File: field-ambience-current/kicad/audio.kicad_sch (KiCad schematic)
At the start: 20 parts, among them J6 Speaker L (PUI AS04008PS, 4R 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, J7 Speaker R (PUI AS04008PS, 4R 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, U3 PCM5102A I²S DAC (TSSOP-20), U4 PAM8403 Class-D Stereo Amp (S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

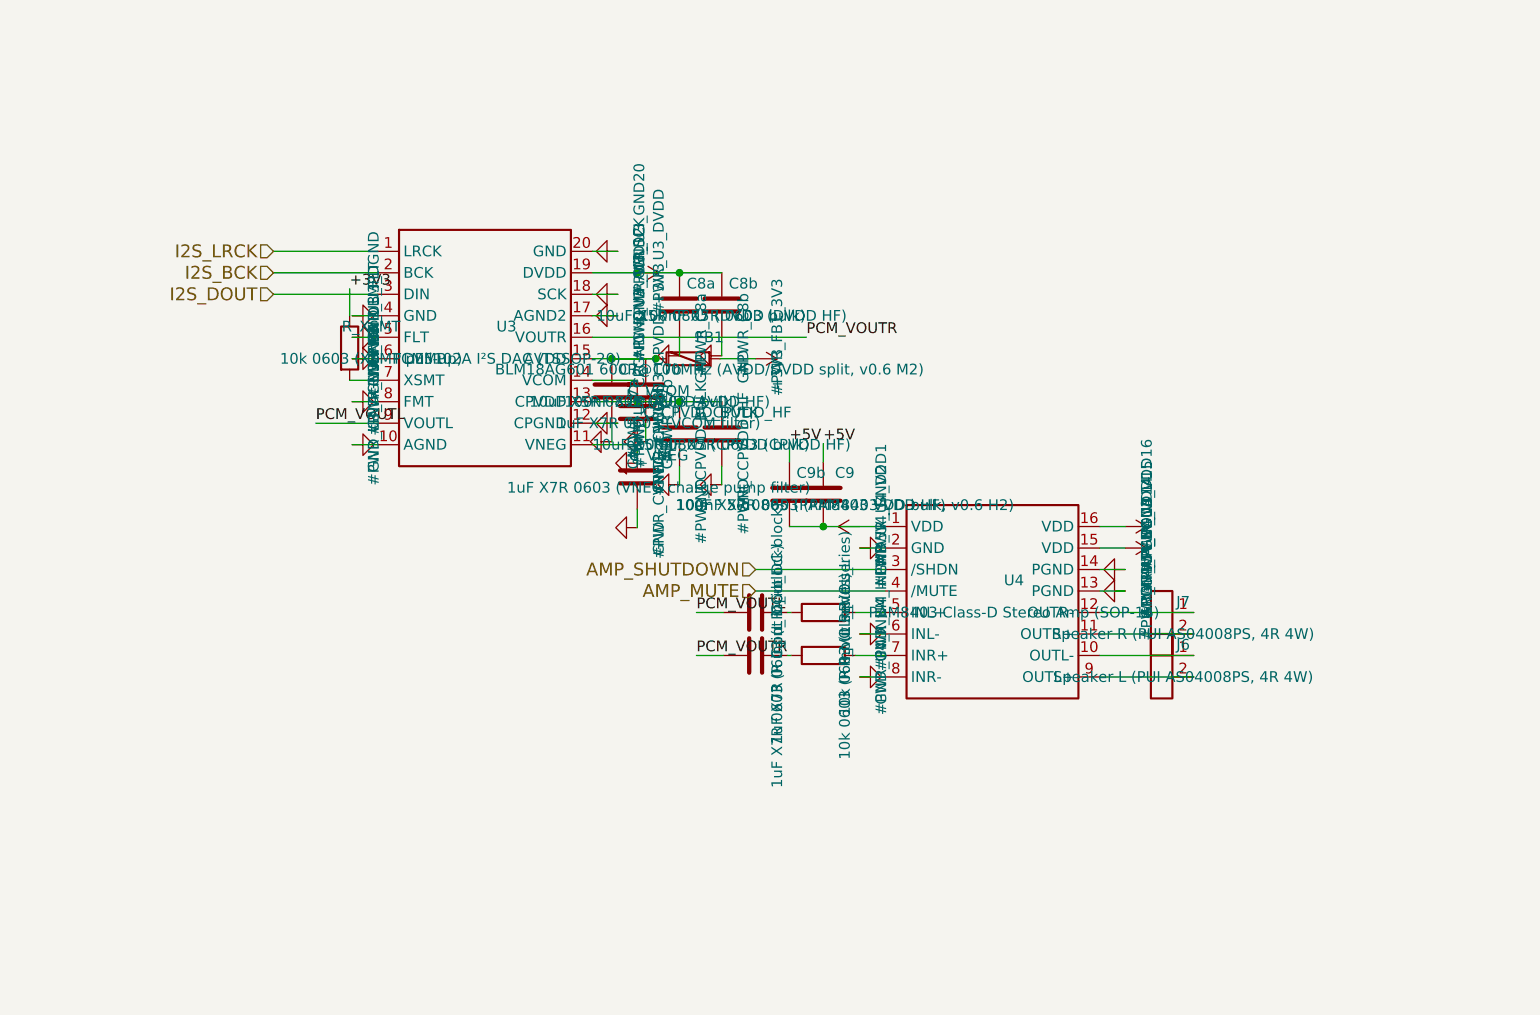
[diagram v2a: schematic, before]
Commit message: Fix PCM5102A and PAM8403 pinouts per official datasheets (Review Fix)
CRITICAL FIX from PR #1 review: Audio-IC symbols had invented pinouts
instead of official datasheet-correct mappings. Any PCB layout from
the previous version would have routed I²S, power and audio-out to
the wrong physical pads.

PCM5102A (TI SLAS859C, TSSOP-20) — corrected pinout:
  Old (wrong)              → New (per TI datasheet)
  Pin 1  = LRCK            → CPVDD
  Pin 2  = BCK             → CAPP (charge pump fly cap +)
  Pin 3  = DIN             → CPGND
  Pin 4  = GND             → CAPM (charge pump fly cap -)
  Pin 5  = FLT             → VNEG (1µF to GND)
  Pin 6  = DEMP            → OUTL (audio out left)
  Pin 7  = XSMT            → OUTR (audio out right)
  Pin 8  = FMT             → AVDD
  Pin 9  = VOUTL           → AGND
  Pin 10 = AGND            → DEMP
  Pin 11 = VNEG            → FLT
  Pin 12 = CPGND           → SCK (3-wire mode = GND)
  Pin 13 = CPVDD           → BCK (bit clock)
  Pin 14 = VCOM            → DIN (data in)
  Pin 15 = AVDD            → LRCK (left/right clock)
  Pin 16 = VOUTR           → FMT (I²S mode = GND)
  Pin 17 = AGND2           → XSMT (pull-up to DVDD)
  Pin 18 = SCK             → LDOO (LDO output, 100nF to GND)
  Pin 19 = DVDD            → DGND
  Pin 20 = GND             → DVDD

Audio Sheet rewritten with full TI reference design:
- CPVDD bulk+HF decoupling (10µF+100nF)
- CAPP-CAPM 1µF fly cap (charge pump)
- VNEG 1µF reservoir to GND
- AVDD via FB1 BLM18AG601 (v0.6 M2 split) + 10µF+100nF
- DVDD 10µF+100nF decoupling
- LDOO 100nF stability cap
- XSMT 10k pull-up to +3V3
- FLT, DEMP, SCK, FMT all tied to GND

PAM8403DR-H (Diodes Inc DS31295, SOIC-16, LCSC C17337) — corrected:
  Pin 1  = OUTL+        (BTL left output, positive)
  Pin 2  = PGND         (Power ground, left)
  Pin 3  = OUTL-        (BTL left output, negative)
  Pin 4  = PVDD         (Power supply, left)
  Pin 5  = /MUTE        (Active LOW mute)
  Pin 6  = VDD          (Internal supply)
  Pin 7  = INL 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
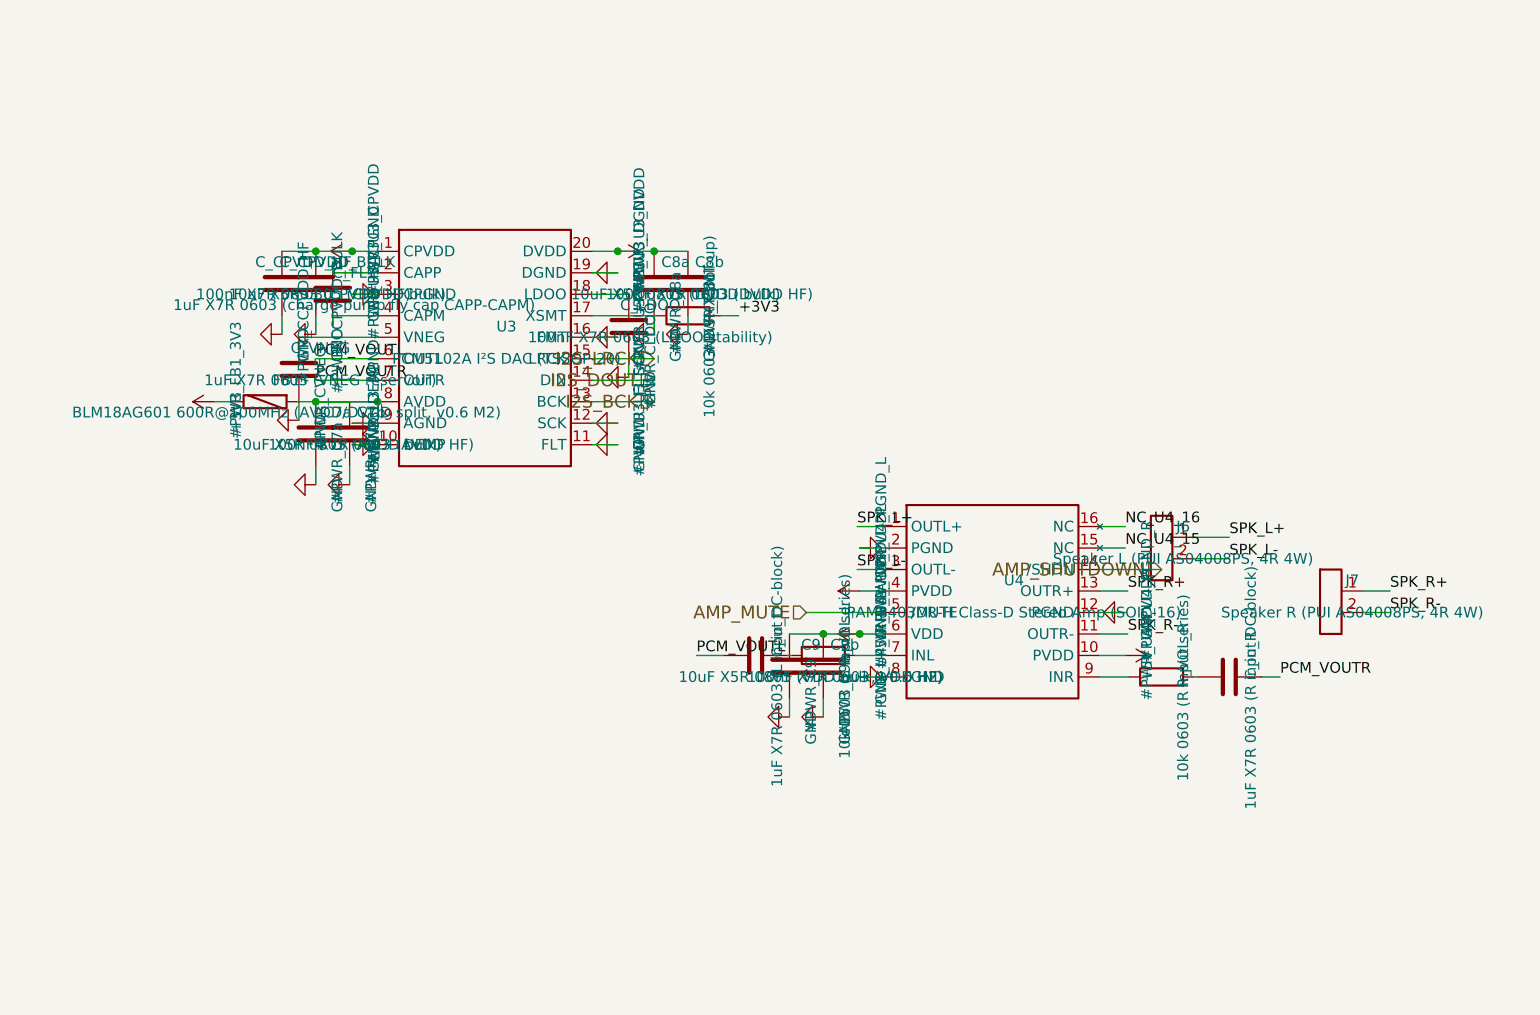
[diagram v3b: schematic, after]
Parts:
- removed C_VCOM: 1uF X7R 0603 (VCOM filter), Capacitor_SMD:C_0603_1608Metric, symbol Device:C
- added C_FLY: 1uF X7R 0603 (charge pump fly cap CAPP-CAPM), Capacitor_SMD:C_0603_1608Metric, symbol Device:C
- added C_LDOO: 100nF X7R 0603 (LDOO stability), Capacitor_SMD:C_0603_1608Metric, symbol Device:C
- C9: value 10uF X5R 0805 (PAM8403 VDD bulk, v0.6 H2) -> 10uF X5R 0805 (VDD bulk, v0.6 H2)
- C9b: value 100nF X7R 0603 (PAM8403 VDD HF) -> 100nF X7R 0603 (VDD HF)
- C_VNEG: value 1uF X7R 0603 (VNEG charge pump filter) -> 1uF X7R 0603 (VNEG reservoir)
- U3: MPN PCM5102A -> PCM5102APWR
- U4: value PAM8403 Class-D Stereo Amp (SOP-16) -> PAM8403DR-H Class-D Stereo Amp (SOIC-16); MPN PAM8403 -> PAM8403DR-H
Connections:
- net +3V3: now also FB1.2, R_XSMT.2, U3.1 (CPVDD), U3.20 (DVDD); no longer FB1.1, R_XSMT.1, U3.13 (CPVDD), U3.19 (DVDD)
- net +5V: now also U4.10 (PVDD), U4.4 (PVDD), U4.6 (VDD); no longer C9.2, C9b.2, U4.1 (VDD), U4.15 (VDD), U4.16 (VDD)
- net AMP_MUTE: now also U4.5 (/MUTE); no longer U4.4 (/MUTE)
- net AMP_SHUTDOWN: now also U4.14 (/SHDN); no longer U4.3 (/SHDN)
- net GND: now also C9.2, C9b.2, U3.16 (FMT), U3.19 (DGND), U3.3 (CPGND), U3.9 (AGND), U4.12 (PGND), C_LDOO.2; no longer C_VNEG.1, U3.17 (AGND2), U3.18 (SCK), U3.20 (GND), U3.4 (GND), U3.5 (FLT), U3.6 (DEMP), U3.8 (FMT), U4.13 (PGND), U4.14 (PGND), U4.6 (INL-)
- net I2S_BCK: now also U3.13 (BCK); no longer U3.2 (BCK)
- net I2S_DOUT: now also U3.14 (DIN); no longer U3.3 (DIN)
- net I2S_LRCK: now also U3.15 (LRCK); no longer U3.1 (LRCK)
- net PCM_VOUTL: now also U3.6 (OUTL); no longer U3.9 (VOUTL)
- net PCM_VOUTR: now also C_in_R.2, U3.7 (OUTR); no longer C_in_R.1, U3.16 (VOUTR)
- net SPK_L+: now reaches J6.1 (Pin_1)
- net SPK_L+: now also U4.1 (OUTL+); no longer U4.10 (OUTL-)
- net SPK_R-: now reaches J7.2 (Pin_2), U4.11 (OUTR-)
- net SPK_R+: now reaches J7.1 (Pin_1)
- net SPK_R+: now also U4.13 (OUTR+); no longer U4.12 (OUTR-)
- net at R_VOL_L.2: now also U4.7 (INL); no longer U4.5 (INL+)
- net at R_VOL_R.2: now also C_in_R.1; no longer U4.7 (INR+)
- net at U4.9 (INR): now also R_VOL_R.1; no longer J6.2 (Pin_2)
- net at C7a.1, C7b.1: now also FB1.1, U3.8 (AVDD); no longer FB1.2, U3.15 (AVDD)
- new net: C_FLY.1, U3.2 (CAPP)
- new net: C_FLY.2, U3.4 (CAPM)
- new net: C_VNEG.1, U3.5 (VNEG)
- new net: C_LDOO.1, U3.18 (LDOO)
- new net: R_XSMT.1, U3.17 (XSMT)
- new net NC_U4_15: U4.15 (NC)
- new net NC_U4_16: U4.16 (NC)
- new net SPK_L-: J6.2 (Pin_2), U4.3 (OUTL-)
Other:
- moved on the sheet: C7a, C7b, C8a, C8b, C9, C9b, C_CPVDD_BULK, C_CPVDD_HF, C_VNEG, C_in_L, C_in_R, FB1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

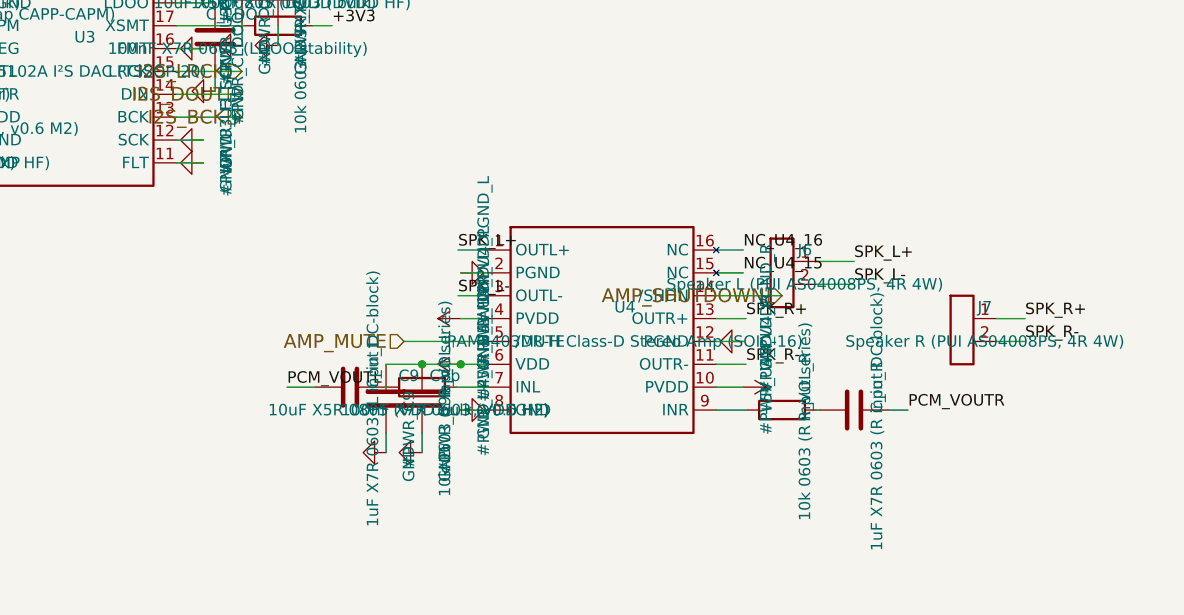
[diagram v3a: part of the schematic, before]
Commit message: Fix PAM8403H pinout using official datasheet PDF (PAM8403H.PDF)
The previous v0.6.1 fix for PAM8403 was based on a wrong DS31295
guess. With the actual Diodes Inc PAM8403H datasheet PDF now in the
repo (PAM8403H.PDF Rev 1-0 Nov 2012), the symbol can be verified
pin-by-pin against the JLCPCB C17337 part.

PAM8403H verified pinout (LCSC C17337):
  Pin 1:  -OUT_L (Left negative output, BTL)
  Pin 2:  PGND
  Pin 3:  +OUT_L (Left positive output, BTL)
  Pin 4:  PVDD
  Pin 5:  MUTE (active LOW)
  Pin 6:  VDD
  Pin 7:  INL
  Pin 8:  VREF  ← bypass cap to GND REQUIRED per datasheet
  Pin 9:  NC
  Pin 10: INR
  Pin 11: GND (analog)
  Pin 12: SHDN (active LOW)
  Pin 13: PVDD
  Pin 14: +OUT_R (Right positive output)
  Pin 15: PGND
  Pin 16: -OUT_R (Right negative output)

Critical errors fixed from v0.6.1:
- OUTL+ / OUTL- polarity was swapped (was on pins 1/3, must be 3/1)
- Pin 8 was wrongly GND, must be VREF (analog reference)
- Pin 9 was wrongly INR, must be NC
- Pin 10 was wrongly PVDD, must be INR
- Pin 11 was wrongly OUTR-, must be GND
- Pin 12 was wrongly PGND, must be SHDN
- Pin 13 was wrongly OUTR+, must be PVDD
- Pin 14 was wrongly /SHDN, must be +OUT_R
- Pin 15 was wrongly NC, must be PGND
- Pin 16 was wrongly NC, must be -OUT_R
- VREF bypass cap was missing — added C_VREF 1µF X7R

audio.kicad_sch U4 wiring completely rewritten to match correct pins.
Component count grew from 84 → 85 (added C_VREF).

SPEC v0.6.2 errata section updated with full PAM8403H pin table.

Verified via analyzer pin_nets dump for U4:
  Pin 1=SPK_L-, Pin 3=SPK_L+, Pin 14=SPK_R+, Pin 16=SPK_R-,
  Pin 4/6/13=+5V, Pin 2/11/15=GND, Pin 5=AMP_MUTE, Pin 12=AMP_SHUTDOWN,
  Pin 7/10=INL/INR, Pin 8=VREF (with C_VREF), Pin 9=NC.

Status: 0 functional errors, 19 warnings, 3 VM-001 false positives.
85 components, 117 nets. Audio path now safe for PCB layout once
mechanical footprint of SOP-16/SOIC-16 is also verified against the
exact JLC-shipped PAM8403H.
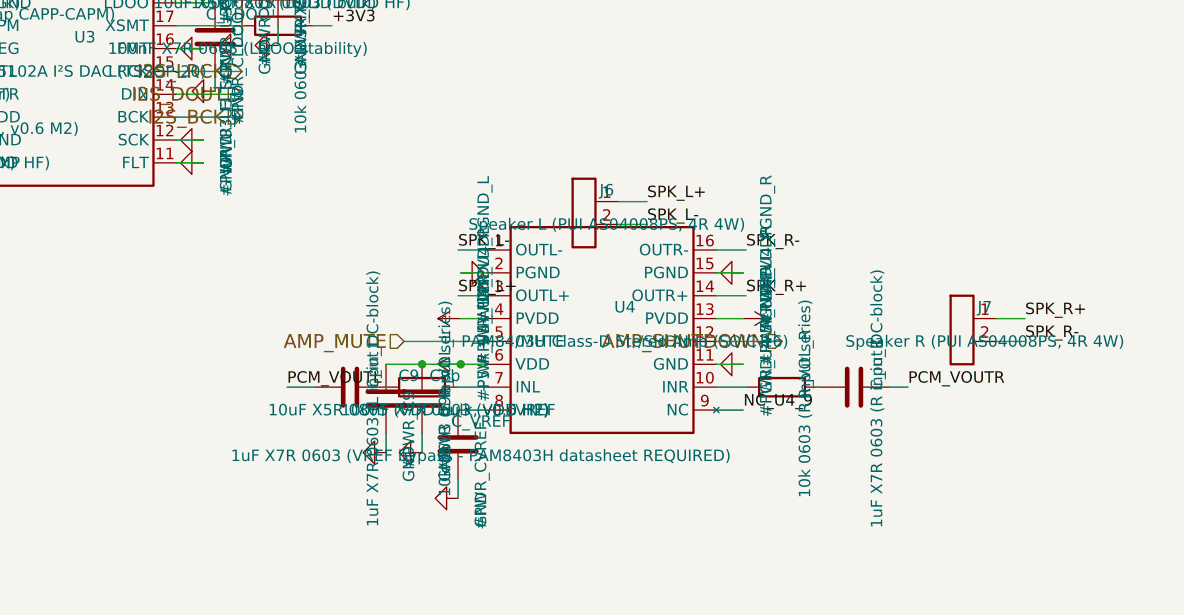
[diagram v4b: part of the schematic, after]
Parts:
- added C_VREF: 1uF X7R 0603 (VREF bypass - PAM8403H datasheet RE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, Capacitor_SMD:C_0603_1608Metric, symbol Device:C
- U4: value PAM8403DR-H Class-D Stereo Amp (SOIC-16) -> PAM8403H Class-D Stereo Amp (SOIC-16); MPN PAM8403DR-H -> PAM8403H
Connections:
- net NC_U4_15 is gone; now on net GND: U4.15 (PGND)
- net NC_U4_16 is gone; now on net SPK_R-: U4.16 (OUTR-)
- net +5V: now also U4.13 (PVDD); no longer U4.10 (PVDD)
- net AMP_SHUTDOWN: now also U4.12 (/SHDN); no longer U4.14 (/SHDN)
- net GND: now also U4.11 (GND), C_VREF.2; no longer U4.12 (PGND), U4.8 (GND)
- net SPK_L+: now also U4.3 (OUTL+); no longer U4.1 (OUTL+)
- net SPK_L-: now also U4.1 (OUTL-); no longer U4.3 (OUTL-)
- net SPK_R+: now also U4.14 (OUTR+); no longer U4.13 (OUTR+)
- net SPK_R-: no longer U4.11 (OUTR-)
- net at R_VOL_R.1: now also U4.10 (INR); no longer U4.9 (INR)
- new net: C_VREF.1, U4.8 (VREF)
- new net NC_U4_9: U4.9 (NC)
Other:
- moved on the sheet: C_in_R, J6, R_VOL_R
